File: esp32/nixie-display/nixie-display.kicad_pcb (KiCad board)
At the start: 2 copper layers, 99.9 x 69.8 mm, 72 parts, among them J1 Conn_01x10_Male, J2 Conn_01x10_Male, Q1 Q_NPN_CBE, Q10 Q_PNP_CBE, Q11 Q_NPN_CBE, Q12 Q_PNP_CBE, Q13 Q_NPN_CBE, Q14 Q_PNP_CBE, Q15 IRLS640, Q2 Q_PNP_CBE, Q3 Q_NPN_CBE, Q4 Q_PNP_CBE, Q5 Q_NPN_CBE, Q6 Q_PNP_CBE, Q7 Q_NPN_CBE, Q8 Q_PNP_CBE, Q9 Q_NPN_CBE, U1 MAX1771, U2 L78L05_TO92

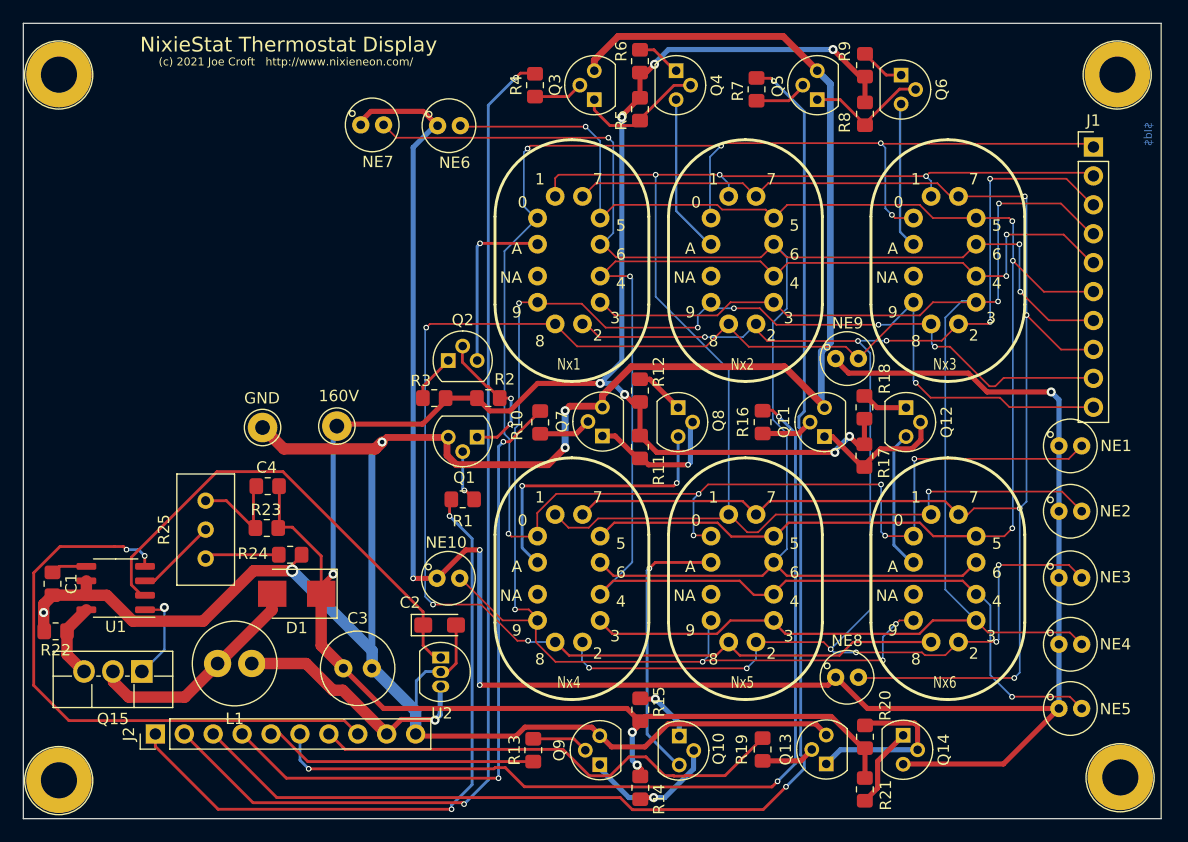
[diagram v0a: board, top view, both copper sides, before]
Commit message: Fixed IN-17 foot prints, Anode drivers, little stuff
[git-p4: depot-paths = "//depot/nixiestat/": change = 320]
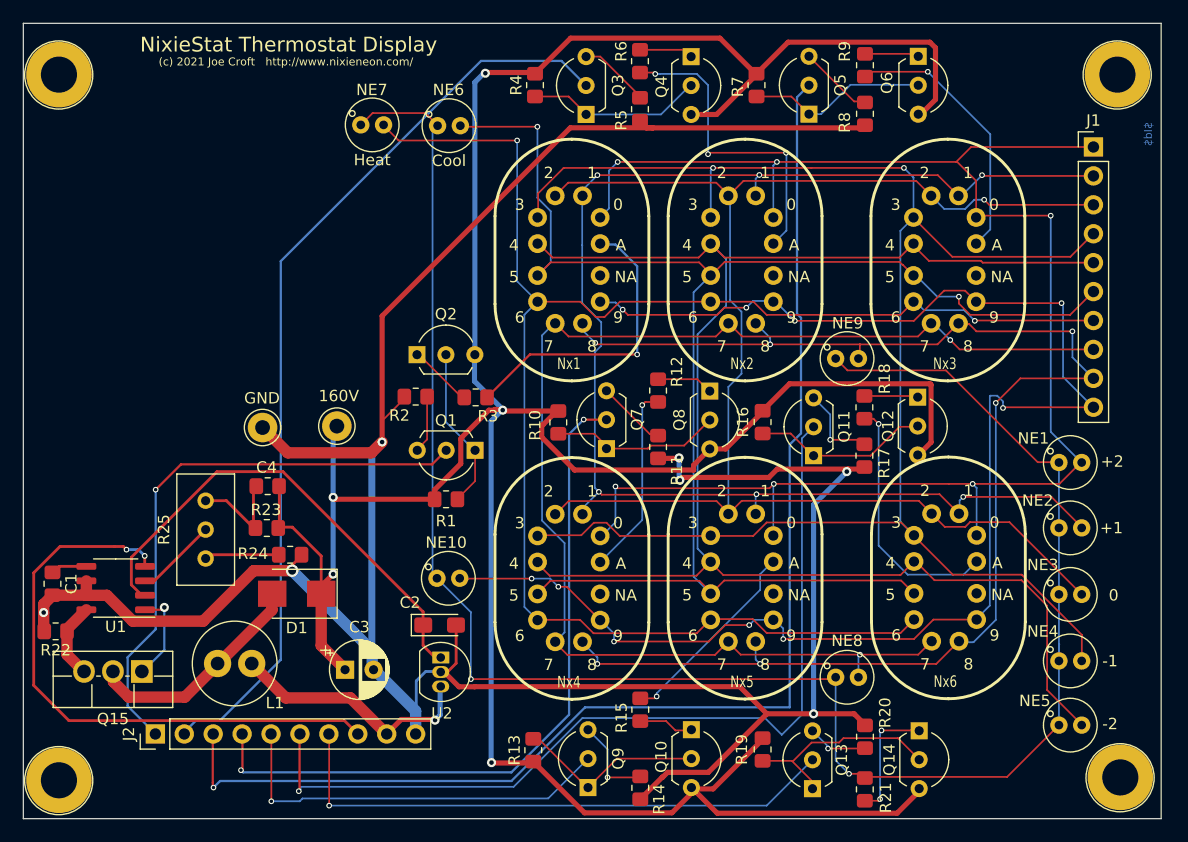
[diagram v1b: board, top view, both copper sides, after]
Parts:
- C3: footprint Capacitor_THT:C_Radial_D6.3mm_H7.0mm_P2.50mm -> Capacitor_THT:CP_Radial_D5.0mm_P2.50mm
- NE1: value Lamp_Neon -> +2
- NE2: value Lamp_Neon -> +1
- NE3: value Lamp_Neon -> 0
- NE4: value Lamp_Neon -> -1
- NE5: value Lamp_Neon -> -2
- NE6: value Lamp_Neon -> Cool
- NE7: value Lamp_Neon -> Heat
- Q1, Q10, Q11, Q12, Q13, Q14, Q2, Q3, Q4, Q5, Q6, Q7, Q8, Q9: footprint Package_TO_SOT_THT:TO-92 -> Package_TO_SOT_THT:TO-92L_Inline_Wide
- R1, R10, R13, R16, R19, R4, R7: value R_US -> 100K
- R11, R14, R17, R2, R20, R5, R8: value R_US -> 3.3K
- R12, R15, R18, R3, R6, R9: value R_US -> 22K
- R21: value R_US -> 35K
- moved R2 6.38 mm to (126.3, 75.5), turned to 180 degrees
- moved R3 3.64 mm to (131.5, 75.6)
- moved Q8 3.14 mm to (152.1, 75.0)
- moved Q2 2.79 mm to (126.4, 71.8)
- moved Q13 2.49 mm to (161.1, 109.9)
- moved Q9 2.26 mm to (141.4, 109.8)
- moved Q6 2.23 mm to (170.4, 45.6)
- moved Q11 1.93 mm to (161.2, 80.7)
- moved Q4 1.81 mm to (150.4, 45.6)
- moved R10 1.59 mm to (138.8, 77.7)
- moved R11 1.59 mm to (147.5, 79.9)
- moved R12 1.59 mm to (147.5, 75.0)
- moved Q3 1.48 mm to (141.2, 50.7)
- moved Q5 1.47 mm to (160.8, 50.7)
- moved Q14 1.46 mm to (170.5, 104.8)
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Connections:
- net Net-(J2-Pad8) renamed HV_DISABLE
- Q1 pad 2: Net-(Q1-Pad2) -> idig0
- Q1 pad 3: GNDREF -> Net-(Q1-Pad3)
- Q10 pad 3: dig4 -> 160V
- Q11 pad 2: Net-(Q11-Pad2) -> idig5
- Q11 pad 3: GNDREF -> Net-(Q11-Pad3)
- Q12 pad 3: dig5 -> 160V
- Q13 pad 2: Net-(Q13-Pad2) -> idig6
- Q13 pad 3: GNDREF -> Net-(Q13-Pad3)
- Q14 pad 3: dig6 -> 160V
- Q2 pad 3: dig0 -> 160V
- Q3 pad 2: Net-(Q3-Pad2) -> idig1
- Q3 pad 3: GNDREF -> Net-(Q3-Pad3)
- Q4 pad 3: dig1 -> 160V
- Q5 pad 2: Net-(Q5-Pad2) -> idig2
- Q5 pad 3: GNDREF -> Net-(Q5-Pad3)
- Q6 pad 3: dig2 -> 160V
- Q7 pad 2: Net-(Q7-Pad2) -> idig3
- Q7 pad 3: GNDREF -> Net-(Q7-Pad3)
- Q8 pad 3: dig3 -> 160V
- Q9 pad 2: Net-(Q9-Pad2) -> idig4
- Q9 pad 3: GNDREF -> Net-(Q9-Pad3)
- R1 pad 1: idig0 -> 160V
- R1 pad 2: Net-(Q1-Pad2) -> Net-(Q1-Pad1)
- R10 pad 1: idig3 -> 160V
- R10 pad 2: Net-(Q7-Pad2) -> Net-(Q7-Pad1)
- R11 pad 1: 160V -> Net-(Q7-Pad3)
- R11 pad 2: Net-(Q7-Pad1) -> GNDREF
- R12 pad 1: 160V -> dig3
- R13 pad 1: idig4 -> 160V
- R13 pad 2: Net-(Q9-Pad2) -> Net-(Q10-Pad2)
- R14 pad 1: 160V -> Net-(Q9-Pad3)
- R14 pad 2: Net-(Q10-Pad2) -> GNDREF
- R15 pad 1: 160V -> dig4
- R16 pad 1: idig5 -> 160V
- R16 pad 2: Net-(Q11-Pad2) -> Net-(Q11-Pad1)
- R17 pad 1: 160V -> Net-(Q11-Pad3)
- R17 pad 2: Net-(Q11-Pad1) -> GNDREF
- R18 pad 1: 160V -> dig5
- R19 pad 1: idig6 -> 160V
- R19 pad 2: Net-(Q13-Pad2) -> Net-(Q13-Pad1)
- R2 pad 1: 160V -> Net-(Q1-Pad3)
- R2 pad 2: Net-(Q1-Pad1) -> GNDREF
- R20 pad 1: 160V -> Net-(Q13-Pad3)
- R20 pad 2: Net-(Q13-Pad1) -> GNDREF
- R21 pad 1: 160V -> dig6
- R3 pad 1: 160V -> dig0
- R4 pad 1: idig1 -> 160V
- R4 pad 2: Net-(Q3-Pad2) -> Net-(Q3-Pad1)
- R5 pad 1: 160V -> Net-(Q3-Pad3)
- R5 pad 2: Net-(Q3-Pad1) -> GNDREF
- R6 pad 1: 160V -> dig1
- R7 pad 1: idig2 -> 160V
- R7 pad 2: Net-(Q5-Pad2) -> Net-(Q5-Pad1)
- R8 pad 1: 160V -> Net-(Q5-Pad3)
- R8 pad 2: Net-(Q5-Pad1) -> GNDREF
- R9 pad 1: 160V -> dig2
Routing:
- net 160V: track 200.2 -> 276.7 mm, vias 10 -> 5
- net /seg7: track 146.1 -> 116.8 mm, vias 4 -> 2
- net /seg0: track 171.7 -> 144.3 mm, vias 10 -> 6
- net GNDREF: track 232.4 -> 256.0 mm, vias 5 -> 7
- net /seg3: track 130.7 -> 146.8 mm
- net dig6: track 182.7 -> 167.2 mm, vias 4 -> 2
- net /seg2: track 145.7 -> 130.7 mm, vias 11 -> 1
- net /seg8: track 138.3 -> 123.4 mm, vias 4 -> 6
- net dig1: track 14.2 -> 27.9 mm, vias 0 -> 3
- net idig1: track 94.5 -> 81.3 mm, vias 2 -> 0
- net dig0: track 15.3 -> 26.4 mm
- net idig4: track 24.1 -> 35.1 mm, vias 0 -> 1
- net /seg1: track 137.3 -> 126.5 mm, vias 4 -> 6
- net dig2: track 13.0 -> 23.5 mm, vias 0 -> 1
- net dig5: track 12.2 -> 22.0 mm, vias 0 -> 1
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
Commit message: Improved grounding New Anode Drivers
[git-p4: depot-paths = "//depot/nixiestat/": change = 328]
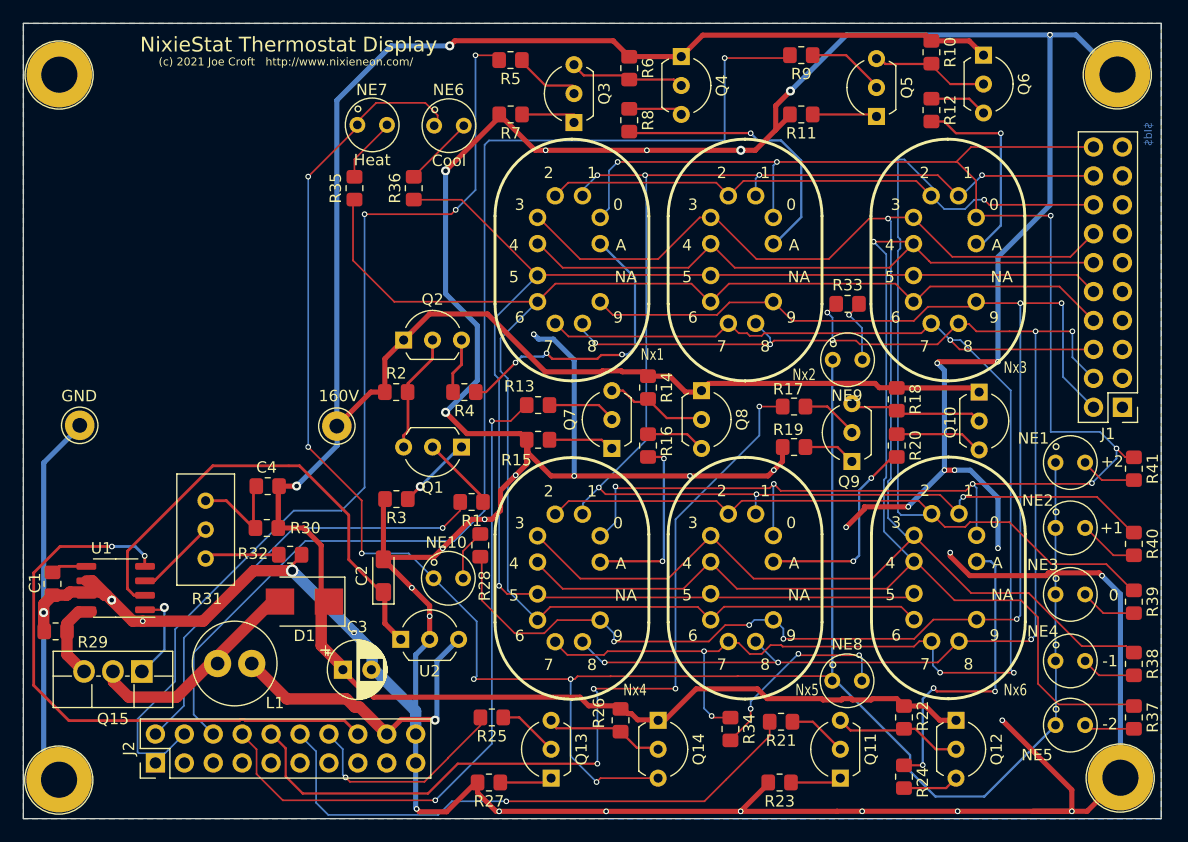
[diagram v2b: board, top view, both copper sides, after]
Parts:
- removed REF** (x4): 4-40-Screw, croftj:4-40-Screw
- added R22: 100K, Resistor_SMD:R_0805_2012Metric_Pad1.20x1.40mm_HandSolder, F.Cu at (169.1, 103.7)
- added R23: 3.3K, Resistor_SMD:R_0805_2012Metric_Pad1.20x1.40mm_HandSolder, F.Cu at (158.2, 109.4)
- added R24: 22K, Resistor_SMD:R_0805_2012Metric_Pad1.20x1.40mm_HandSolder, F.Cu at (169.1, 108.9)
- added R25: 3.3K, Resistor_SMD:R_0805_2012Metric_Pad1.20x1.40mm_HandSolder, F.Cu at (132.9, 103.7)
- added R26: 100K, Resistor_SMD:R_0805_2012Metric_Pad1.20x1.40mm_HandSolder, F.Cu at (144.2, 103.9)
- added R27: 3.3K, Resistor_SMD:R_0805_2012Metric_Pad1.20x1.40mm_HandSolder, F.Cu at (132.7, 109.4)
- added R28: 100K, Resistor_SMD:R_0805_2012Metric_Pad1.20x1.40mm_HandSolder, F.Cu at (131.9, 88.5)
- added R33: 100K, Resistor_SMD:R_0805_2012Metric_Pad1.20x1.40mm_HandSolder, F.Cu at (164.2, 67.3)
- added R34: 100K, Resistor_SMD:R_0805_2012Metric_Pad1.20x1.40mm_HandSolder, F.Cu at (153.9, 104.7)
- added R35: 100K, Resistor_SMD:R_0805_2012Metric_Pad1.20x1.40mm_HandSolder, F.Cu at (120.9, 57.2)
- added R36: 100K, Resistor_SMD:R_0805_2012Metric_Pad1.20x1.40mm_HandSolder, F.Cu at (126.1, 57.2)
- added R37: 100K, Resistor_SMD:R_0805_2012Metric_Pad1.20x1.40mm_HandSolder, F.Cu at (189.3, 103.7)
- added R38: 100K, Resistor_SMD:R_0805_2012Metric_Pad1.20x1.40mm_HandSolder, F.Cu at (189.3, 99.0)
- added R39: 100K, Resistor_SMD:R_0805_2012Metric_Pad1.20x1.40mm_HandSolder, F.Cu at (189.3, 93.5)
- added R40: 100K, Resistor_SMD:R_0805_2012Metric_Pad1.20x1.40mm_HandSolder, F.Cu at (189.3, 88.4)
- added R41: 100K, Resistor_SMD:R_0805_2012Metric_Pad1.20x1.40mm_HandSolder, F.Cu at (189.3, 81.8)
- added SH1: ScrewHole, croftj:4-40-Screw, F.Cu at (95.2, 42.8)
- added SH2: ScrewHole, croftj:4-40-Screw, F.Cu at (95.2, 104.7)
- added SH3: ScrewHole, croftj:4-40-Screw, F.Cu at (188.1, 42.8)
- added SH4: ScrewHole, croftj:4-40-Screw, F.Cu at (188.4, 104.5)
- J1, J2: value Conn_01x10_Male -> Conn_02x10_Odd_Even; footprint Connector_PinHeader_2.54mm:PinHeader_1x10_P2.54mm_Vertical -> Connector_PinHeader_2.54mm:PinHeader_2x10_P2.54mm_Vertical
- Q1, Q11, Q13, Q3, Q5, Q7, Q9: value Q_NPN_CBE -> MPSA42
- Q10, Q12, Q14, Q2, Q4, Q6, Q8: value Q_PNP_CBE -> MPSA92
- R1, R13, R19, R7: value 100K -> 3.3K
- R14, R2: value 3.3K -> 100K
- R15, R3, R9: value 22K -> 3.3K
- R16, R4: value 100K -> 22K
- R18, R6: value 22K -> 100K
- R20, R8: value 3.3K -> 22K
- R21: value 35K -> 3.3K
- U2: footprint Package_TO_SOT_THT:TO-92_Inline -> Package_TO_SOT_THT:TO-92_Inline_Wide
- moved R10 46.2 mm to (171.5, 45.2)
- moved Q10 39.0 mm to (175.7, 75.1)
- moved Q9 36.8 mm to (164.6, 81.2)
- moved R14 35.2 mm to (146.7, 74.7)
- moved R12 34.4 mm to (171.5, 50.3)
- moved R11 31.8 mm to (160.1, 50.7), turned to 180 degrees
- moved R13 30.3 mm to (137.0, 76.2), turned to 180 degrees
- moved Q12 28.6 mm to (173.7, 103.9)
- moved Q11 28.4 mm to (163.5, 109.0)
- moved R4 27.7 mm to (130.5, 75.1), turned to 180 degrees
- moved R19 26.7 mm to (159.5, 79.9), turned to 180 degrees
- moved R20 25.7 mm to (168.5, 79.8)
- moved R15 25.3 mm to (137.0, 79.3), turned to 180 degrees
- moved J1 23.0 mm to (188.3, 76.4), turned to 180 degrees
- moved Q13 23.0 mm to (138.1, 109.0)
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- renumbered R22 to R29, R23 to R30, R25 to R31, R24 to R32
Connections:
- J1 pad 1: /seg0 -> GNDREF
- J1 pad 10: /seg9 -> /seg5
- J1 pad 2: /seg1 -> /seg9
- J1 pad 3: /seg2 -> GNDREF
- J1 pad 4: /seg3 -> /seg8
- J1 pad 5: /seg4 -> GNDREF
- J1 pad 6: /seg5 -> /seg7
- J1 pad 7: /seg6 -> GNDREF
- J1 pad 8: /seg7 -> /seg6
- J1 pad 9: /seg8 -> GNDREF
- J2 pad 1: idig0 -> GNDREF
- J2 pad 10: GNDREF -> idig4
- J2 pad 2: idig1 -> idig0
- J2 pad 3: idig2 -> GNDREF
- J2 pad 4: idig3 -> idig1
- J2 pad 5: idig4 -> GNDREF
- J2 pad 6: idig5 -> idig2
- J2 pad 7: idig6 -> GNDREF
- J2 pad 8: HV_DISABLE -> idig3
- J2 pad 9: VCC -> GNDREF
- NE1 pad 2: /seg0 -> Net-(NE1-Pad2)
- NE10 pad 2: /seg9 -> Net-(NE10-Pad2)
- NE2 pad 2: /seg1 -> Net-(NE2-Pad2)
- NE3 pad 2: /seg2 -> Net-(NE3-Pad2)
- NE4 pad 2: /seg3 -> Net-(NE4-Pad2)
- NE5 pad 2: /seg4 -> Net-(NE5-Pad2)
- NE6 pad 2: /seg5 -> Net-(NE6-Pad2)
- NE7 pad 2: /seg6 -> Net-(NE7-Pad2)
- NE8 pad 2: /seg7 -> Net-(NE8-Pad2)
- NE9 pad 2: /seg8 -> Net-(NE9-Pad2)
- Q1 pad 2: idig0 -> Net-(Q1-Pad2)
- Q10 pad 1: Net-(Q10-Pad1) -> 160V
- Q10 pad 3: 160V -> Net-(Q10-Pad3)
- Q11 pad 2: idig5 -> Net-(Q11-Pad2)
- Q12 pad 1: Net-(Q12-Pad1) -> 160V
- Q12 pad 2: Net-(Q11-Pad1) -> Net-(Q11-Pad3)
- Q12 pad 3: 160V -> Net-(Q12-Pad3)
- Q13 pad 2: idig6 -> Net-(Q13-Pad2)
- Q14 pad 1: Net-(Q14-Pad1) -> 160V
- Q14 pad 2: Net-(Q13-Pad1) -> Net-(Q13-Pad3)
- Q14 pad 3: 160V -> dig6
- Q2 pad 1: Net-(Q2-Pad1) -> 160V
- Q2 pad 2: Net-(Q1-Pad1) -> Net-(Q1-Pad3)
- Q2 pad 3: 160V -> Net-(Q2-Pad3)
- Q3 pad 2: idig1 -> Net-(Q3-Pad2)
- Q4 pad 1: Net-(Q4-Pad1) -> 160V
- Q4 pad 2: Net-(Q3-Pad1) -> Net-(Q3-Pad3)
- Q4 pad 3: 160V -> Net-(Q4-Pad3)
- Q5 pad 2: idig2 -> Net-(Q5-Pad2)
- Q6 pad 1: Net-(Q6-Pad1) -> 160V
- Q6 pad 2: Net-(Q5-Pad1) -> Net-(Q5-Pad3)
- Q6 pad 3: 160V -> Net-(Q6-Pad3)
- Q7 pad 2: idig3 -> Net-(Q7-Pad2)
- Q8 pad 1: Net-(Q8-Pad1) -> 160V
- Q8 pad 2: Net-(Q7-Pad1) -> Net-(Q7-Pad3)
- Q8 pad 3: 160V -> Net-(Q8-Pad3)
- Q9 pad 1: Net-(Q10-Pad2) -> Net-(Q9-Pad1)
- Q9 pad 2: idig4 -> Net-(Q9-Pad2)
- Q9 pad 3: Net-(Q9-Pad3) -> Net-(Q10-Pad2)
- R1 pad 1: 160V -> Net-(Q1-Pad2)
- R1 pad 2: Net-(Q1-Pad1) -> idig0
- R10 pad 2: Net-(Q7-Pad1) -> Net-(Q5-Pad3)
- R11 pad 1: Net-(Q7-Pad3) -> Net-(Q5-Pad1)
- R12 pad 1: dig3 -> dig2
- R12 pad 2: Net-(Q8-Pad1) -> Net-(Q6-Pad3)
- R13 pad 1: 160V -> Net-(Q7-Pad2)
- R13 pad 2: Net-(Q10-Pad2) -> idig3
- R14 pad 1: Net-(Q9-Pad3) -> 160V
- R14 pad 2: GNDREF -> Net-(Q7-Pad3)
- R15 pad 1: dig4 -> Net-(Q7-Pad1)
- R15 pad 2: Net-(Q10-Pad1) -> GNDREF
- R16 pad 1: 160V -> dig3
- R16 pad 2: Net-(Q11-Pad1) -> Net-(Q8-Pad3)
- R17 pad 1: Net-(Q11-Pad3) -> Net-(Q9-Pad2)
- R17 pad 2: GNDREF -> idig4
- R18 pad 1: dig5 -> 160V
- R18 pad 2: Net-(Q12-Pad1) -> Net-(Q10-Pad2)
- R19 pad 1: 160V -> Net-(Q9-Pad1)
- R19 pad 2: Net-(Q13-Pad1) -> GNDREF
- R2 pad 1: Net-(Q1-Pad3) -> 160V
- R2 pad 2: GNDREF -> Net-(Q1-Pad3)
- R20 pad 1: Net-(Q13-Pad3) -> dig4
- R20 pad 2: GNDREF -> Net-(Q10-Pad3)
- R21 pad 1: dig6 -> Net-(Q11-Pad2)
- R21 pad 2: Net-(Q14-Pad1) -> idig5
- R3 pad 1: dig0 -> Net-(Q1-Pad1)
- R3 pad 2: Net-(Q2-Pad1) -> GNDREF
- R4 pad 1: 160V -> dig0
- R4 pad 2: Net-(Q3-Pad1) -> Net-(Q2-Pad3)
- R5 pad 1: Net-(Q3-Pad3) -> Net-(Q3-Pad2)
- R5 pad 2: GNDREF -> idig1
- R6 pad 1: dig1 -> 160V
- R6 pad 2: Net-(Q4-Pad1) -> Net-(Q3-Pad3)
- R7 pad 1: 160V -> Net-(Q3-Pad1)
- R7 pad 2: Net-(Q5-Pad1) -> GNDREF
- R8 pad 1: Net-(Q5-Pad3) -> dig1
- R8 pad 2: GNDREF -> Net-(Q4-Pad3)
- R9 pad 1: dig2 -> Net-(Q5-Pad2)
- R9 pad 2: Net-(Q6-Pad1) -> idig2
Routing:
- net GNDREF: track 256.0 -> 459.7 mm, vias 7 -> 38
- net idig4: track 35.1 -> 76.9 mm, vias 1 -> 4
- net 160V: track 276.7 -> 244.9 mm, vias 5 -> 2
- net idig6: track 50.3 -> 19.1 mm
- net idig5: track 79.1 -> 50.8 mm
- net dig6: track 167.2 -> 194.3 mm, vias 2 -> 6
- net Net-(NE8-Pad2): track 0.00 -> 17.9 mm, vias 0 -> 3
- net /seg7: track 116.8 -> 133.9 mm, vias 2 -> 5
- net /seg2: track 130.7 -> 144.9 mm
- net Net-(Q13-Pad1): track 18.5 -> 4.49 mm
- net idig0: track 50.3 -> 39.0 mm
- net Net-(Q11-Pad1): track 15.4 -> 4.36 mm
- net Net-(Q3-Pad1): track 15.4 -> 4.59 mm
- net Net-(Q14-Pad1): track 10.6 -> 0.00 mm, vias 2 -> 0
- net Net-(Q5-Pad1): track 15.9 -> 5.66 mm
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- added copper zone on B.Cu, net GNDREF
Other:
- net class HiVolt added: clearance 0.762, trace_width 0.25, via_dia 0.8, via_drill 0.4
- rule via_min_size: 0.4 -> 0.3
